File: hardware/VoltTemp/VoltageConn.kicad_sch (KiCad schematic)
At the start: 26 parts, among them J1 Conn_01x11, J7 Conn_01x04

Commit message: schematic mostly done
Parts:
- removed C10, C11, C6, C7, C8, C9: 1μF, Capacitor_SMD:C_0805_2012Metric, symbol Device:C_Small
- removed J1: Conn_01x11, symbol Connector_Generic:Conn_01x11
- removed R12, R13, R14, R15, R16: 0Ω, Resistor_SMD:R_0805_2012Metric, symbol Device:R
- removed R17, R18, R19, R20, R21, R22: 100Ω, Resistor_SMD:R_0805_2012Metric, symbol Device:R
- added C34, C35, C36, C37, C38, C39: 1uF, Capacitor_SMD:C_0603_1608Metric_Pad1.08x0.95mm_HandSolder, symbol Device:C
- added J11: Conn_01x07, VoltTemp:1053131107, symbol Connector_Generic:Conn_01x07
- added R53, R54, R55, R56, R57, R58: 100Ω, Resistor_SMD:R_0603_1608Metric_Pad0.98x0.95mm_HandSolder, symbol Device:R
- added TP16, TP17, TP18, TP19, TP20, TP21: TestPoint, TestPoint:TestPoint_Pad_1.5x1.5mm, symbol Connector:TestPoint
- F10, F11, F12, F7, F8, F9: footprint UTSVT_Special:ptc_fuse_FUSC1607X75N -> VoltTemp:ptc_fuse_FUSC1607X75N
- J7: footprint (none) -> VoltTemp:1053132104; P/N (none) -> 1053132104
- R23: footprint Resistor_SMD:R_0805_2012Metric -> Resistor_SMD:R_0603_1608Metric_Pad0.98x0.95mm_HandSolder; P/N SMD_0805 -> (none)
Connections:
- net 1&2COM: now also R54.2
- net 2&3COM: now also R55.2
- net 3&4COM_Out: now also R56.2
- net 4&5COM: now also R57.2
- net GND2: now also C34.1, C35.2, R53.2
- net VC0: now also C34.2, R53.1, TP16.1
- net VC1: now also C35.1, C36.2, R54.1, TP17.1
- net VC2: now also C36.1, C37.2, R55.1, TP18.1
- net VC3: now also C37.1, C38.2, R56.1, TP19.1
- net VC4: now also C38.1, C39.2, R57.1, TP20.1
- net VC5: now also C39.1, R58.1, TP21.1
- net last_cell: now also R58.2
- net at F8.1: now also J11.2 (Pin_2)
- net at F11.1: now also J11.5 (Pin_5)
- net at F10.1: now also J11.4 (Pin_4)
- net at F7.1: now also J11.1 (Pin_1)
- net at F12.1: now also J11.7 (Pin_7)
- net at F9.1: now also J11.3 (Pin_3)
- no-connect marks 6 -> 2
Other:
- moved on the sheet: F10, F11, F12, F7, F8, F9

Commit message: layout
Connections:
- net at J11.2 (Pin_2): no longer F8.1
- net at J11.1 (Pin_1): now also F12.1; no longer F7.1
- net 1&2COM_ext: now reaches J11.3 (Pin_3)
- net 1&2COM_ext: now also F11.1; no longer F9.1
- net 2&3COM_ext: now reaches F10.1, J11.4 (Pin_4)
- net 3&4COM_ext: now reaches J11.5 (Pin_5)
- net 3&4COM_ext: now also F9.1; no longer F11.1
- net 4&5COM_ext: now reaches J11.6 (Pin_6)
- net 4&5COM_ext: now also F8.1
- net last_cell_ext: now reaches J11.7 (Pin_7)
- net last_cell_ext: now also F7.1; no longer F12.1
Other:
- moved on the sheet: F10, F11, F12, F7, F8, F9

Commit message: most layout done
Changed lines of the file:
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@@
+	)
+	(junction
+		(at 125.73 44.45)
+		(diameter 0)
+		(color 0 0 0 0)
 	)
 	(junction
@@
 	(wire
 		(pts
+			(xy 125.73 39.37) (xy 125.73 44.45)
+		)
+		(stroke
+			(width 0)
+			(type default)
+		)
+	)
+	(wire
+		(pts
 			(xy 71.12 45.72) (xy 86.36 45.72)
 		)
@@
 	(wire
 		(pts
-			(xy 114.3 44.45) (xy 127 44.45)
+			(xy 114.3 44.45) (xy 125.73 44.45)
 		)
 		(stroke
@@
 	(wire
 		(pts
+			(xy 125.73 44.45) (xy 127 44.45)
+		)
+		(stroke
+			(width 0)
+			(type default)
+		)
+	)
+	(wire
+		(pts
 			(xy 114.3 59.69) (xy 127 59.69)
 		)
@@
 		(pts
 			(xy 134.62 52.07) (xy 135.89 52.07)
+		)
+		(stroke
+			(width 0)
+			(type default)
+		)
+	)
+	(wire
+		(pts
+			(xy 123.19 39.37) (xy 125.73 39.37)
 		)
 		(stroke
@@
 		)
 	)
+	(hierarchical_label "last_cell"
+		(shape output)
+		(at 123.19 39.37 180)
+		(effects
+			(font
+				(size 1.27 1.27)
+			)
+			(justify right)
+		)
+	)

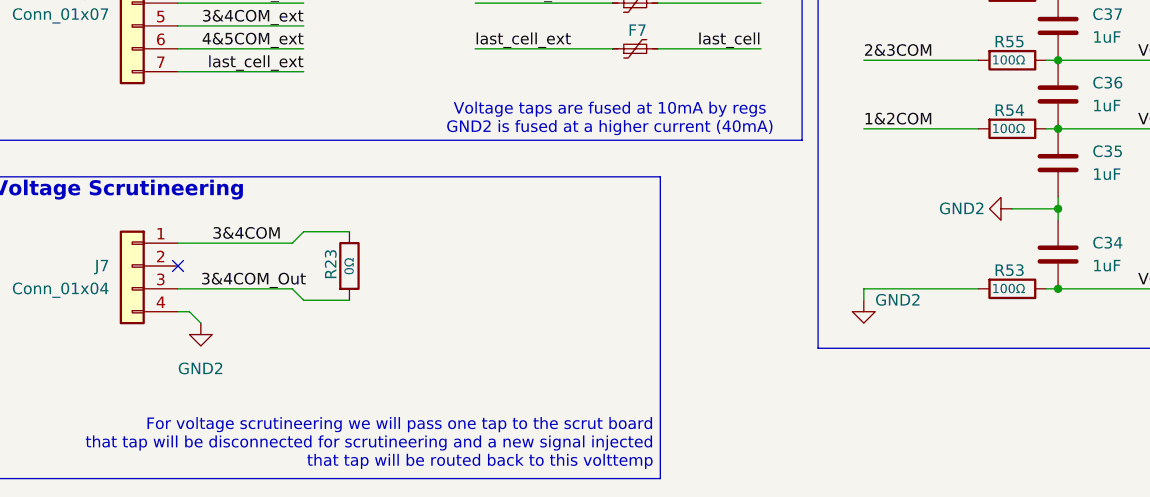
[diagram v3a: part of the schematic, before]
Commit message: add thermistor test board, just need to route volttemp testpoints
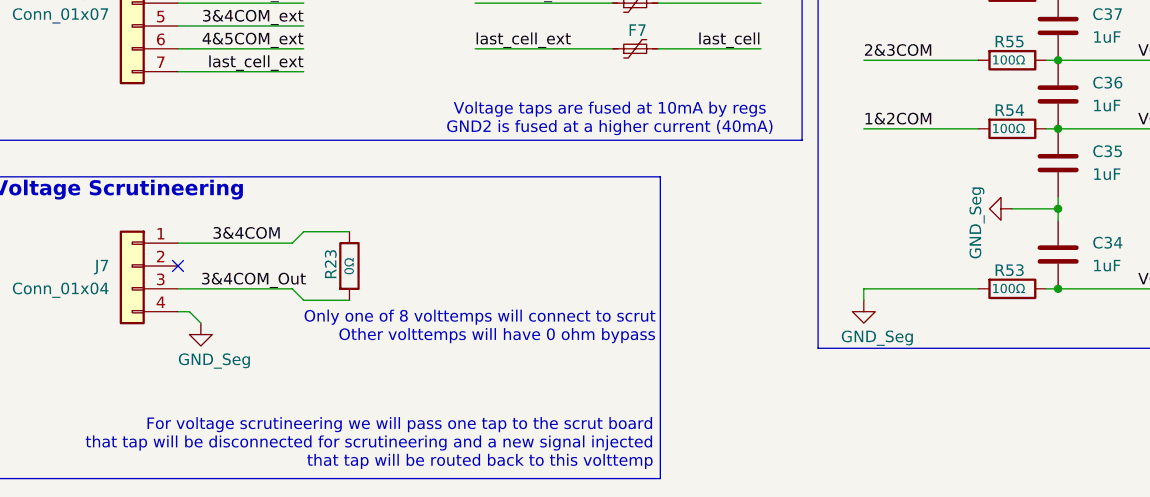
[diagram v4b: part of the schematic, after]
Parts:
- F10, F11, F7, F8, F9: P/N FUSC1607X75N -> PTSLR06038V075
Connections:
- net GND2: no longer C34.1, C35.2, J7.4 (Pin_4), R53.2
- new net GND_Seg: C34.1, C35.2, J7.4 (Pin_4), R53.2
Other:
- note added: "Only one of 8 volttemps will connect to scrut Other volttemps will have 0 ohm bypass"

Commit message: ravi shah
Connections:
- net GND2 is gone; now on net GND_Seg: F12.2

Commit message: Bom (#3)
* bom

* bom for cell sim and thermistor

* stopped displaying part numbers in schematic
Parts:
- J11: P/N (none) -> 1053131107
- R23: P/N (none) -> SFR03EZPJ000

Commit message: this is the staircase board :(
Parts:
- removed J7: Conn_01x04, VoltTemp:1053132104, symbol Connector_Generic:Conn_01x04
- removed R23: 0Ω, Resistor_SMD:R_0603_1608Metric_Pad0.98x0.95mm_HandSolder, symbol Device:R
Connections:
- net 1&2COM_ext: now also J11.5 (Pin_5); no longer J11.3 (Pin_3)
- net 3&4COM_ext: now also J11.3 (Pin_3); no longer J11.5 (Pin_5)
- net 4&5COM_ext: now also J11.2 (Pin_2); no longer J11.6 (Pin_6)
- net last_cell_ext: now also J11.1 (Pin_1); no longer J11.7 (Pin_7)
- net at F12.1: now also J11.7 (Pin_7); no longer J11.1 (Pin_1)
- net 3&4COM renamed 3&4Com
- net 3&4COM_Out renamed 3&4Com_Out
- no-connect marks 2 -> 1
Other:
- note removed: "For voltage scrutineering we will pass one tap to the scrut board that tap will be disconnected for scrutineering and a new signal injected that tap will be routed back to this volttemp"
- note removed: "Only one of 8 volttemps will connect to scrut Other volttemps will have 0 ohm bypass"
- note removed: "Voltage Scrutineering"
- moved on the sheet: F12, J11
